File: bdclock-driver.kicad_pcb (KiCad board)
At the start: 2 copper layers, 34 parts, among them J1 PWR, J2 Ctrl, J3 Kathodes, J4 Anodes A, J5 Anodes B, J6 Anodes C, U1 NE555P, U2 LM7805_TO220, U3 74HC4017, U4 74HC595, U5 74HC595, U6 74HC595, U7 74LS138, U8 74LS138

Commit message: :hammer: Improve PCB layout
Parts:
- added REF**: MountingHole_3.2mm_M3, MountingHole:MountingHole_3.2mm_M3, F.Cu at (225.6, 101.6)
- added REF**: MountingHole_3.2mm_M3, MountingHole:MountingHole_3.2mm_M3, F.Cu at (123.6, 101.6)
- moved J1 26.3 mm to (128.2, 72.8), turned to 180 degrees
- moved C4 21.8 mm to (128.9, 96.0)
- moved D1 13.2 mm to (125.2, 92.5), turned to 90 degrees
- moved D2 11.6 mm to (121.4, 82.3), turned to -90 degrees
- moved J5 8.67 mm to (180.4, 98.4)
- moved J6 8.67 mm to (202.0, 98.4)
- moved J3 8.67 mm to (138.4, 98.4)
- moved J4 8.67 mm to (159.1, 98.4)
- moved U2 6.02 mm to (128.4, 84.2), turned to -90 degrees
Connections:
- R3 pad 1: ROW1 -> ROW3
- R4 pad 1: ROW2 -> ROW1
- R5 pad 1: ROW3 -> ROW2
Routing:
- net VCC: track 0.00 -> 185.2 mm, vias 0 -> 1
- net CLK: track 37.1 -> 69.4 mm, vias 0 -> 2
- net Net-(D1-K): track 0.00 -> 22.5 mm
- net ROW3: track 54.2 -> 74.7 mm, vias 1 -> 3
- net Net-(U3-Q3): track 0.00 -> 15.9 mm
- net A2: track 40.8 -> 56.0 mm
- net ROW2: track 34.0 -> 47.1 mm, vias 1 -> 2
- net Net-(U5-QH'): track 19.1 -> 31.3 mm, vias 0 -> 1
- net Net-(D1-A): track 0.00 -> 10.3 mm
- net Net-(U1-THR): track 31.0 -> 23.4 mm
- net Net-(J4-Pin_2): track 60.1 -> 67.6 mm, vias 1 -> 0
- net Net-(J4-Pin_3): track 53.4 -> 60.3 mm, vias 1 -> 0
- net Net-(J4-Pin_1): track 66.9 -> 73.5 mm, vias 1 -> 0
- net Net-(J5-Pin_1): track 38.3 -> 44.9 mm, vias 1 -> 0
- net Net-(J4-Pin_4): track 47.1 -> 53.4 mm, vias 1 -> 0
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- added copper zone on B.Cu, net GND
- added copper zone on F.Cu, net GND
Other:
- board outline added: 112.5 x 45.2 mm

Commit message: :art: Finalize the PCB layout
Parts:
- moved R5 6.22 mm to (152.7, 86.9)
- moved J1 4.38 mm to (125.5, 69.4), turned to -90 degrees
- moved R3 3.18 mm to (152.7, 83.8)
- moved R4 3.05 mm to (152.7, 80.8)
- moved C12 1.27 mm to (141.8, 81.9)
- moved C7 0.51 mm to (134.1, 84.3)
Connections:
- R3 pad 1: ROW3 -> ROW1
- R4 pad 1: ROW1 -> ROW2
- R5 pad 1: ROW2 -> ROW3
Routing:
- net Net-(J3-Pin_3): track 19.2 -> 13.7 mm
- net Net-(J3-Pin_2): track 15.3 -> 19.4 mm
- net Net-(J3-Pin_1): track 14.2 -> 17.3 mm
- net Net-(D1-A): track 10.3 -> 8.03 mm
- net /RST: track 67.9 -> 69.2 mm
- net VCC: track 185.2 -> 186.4 mm
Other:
- outline, holes or cut-outs redrawn
- board text added: "+9V"
- board text added: "A1"
- board text added: "A12"
- board text added: "Bulb Dial Clock Driver"
- board text added: "GND"
- board text added: "K1 H"
- board text added: "K2 M"
- board text added: "K3 S"
- board text added: "https://github.com/penguineer/bdclock-driver"
- board text added: "v1"

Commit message: :art: Geographical renumeration of all components
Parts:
- moved R4 0.13 mm to (152.7, 83.9)
- moved R6 0.13 mm to (152.7, 87.0)
- moved R3 0.13 mm to (152.7, 80.9)
- renumbered C11 to C1, C12 to C10, C7 to C11, C4 to C12, C10 to C2, C1 to C3, C3 to C4, C8 to C7, C9 to C8, C2 to C9, D2 to D1, D1 to D2, J2 to J1, J1 to J2, R2 to R1, R1 to R2, R4 to R3, R3 to R4, R6 to R5, R5 to R6, U3 to U2, U4 to U3, U5 to U4, U6 to U5, U7 to U6, U8 to U7, U2 to U8

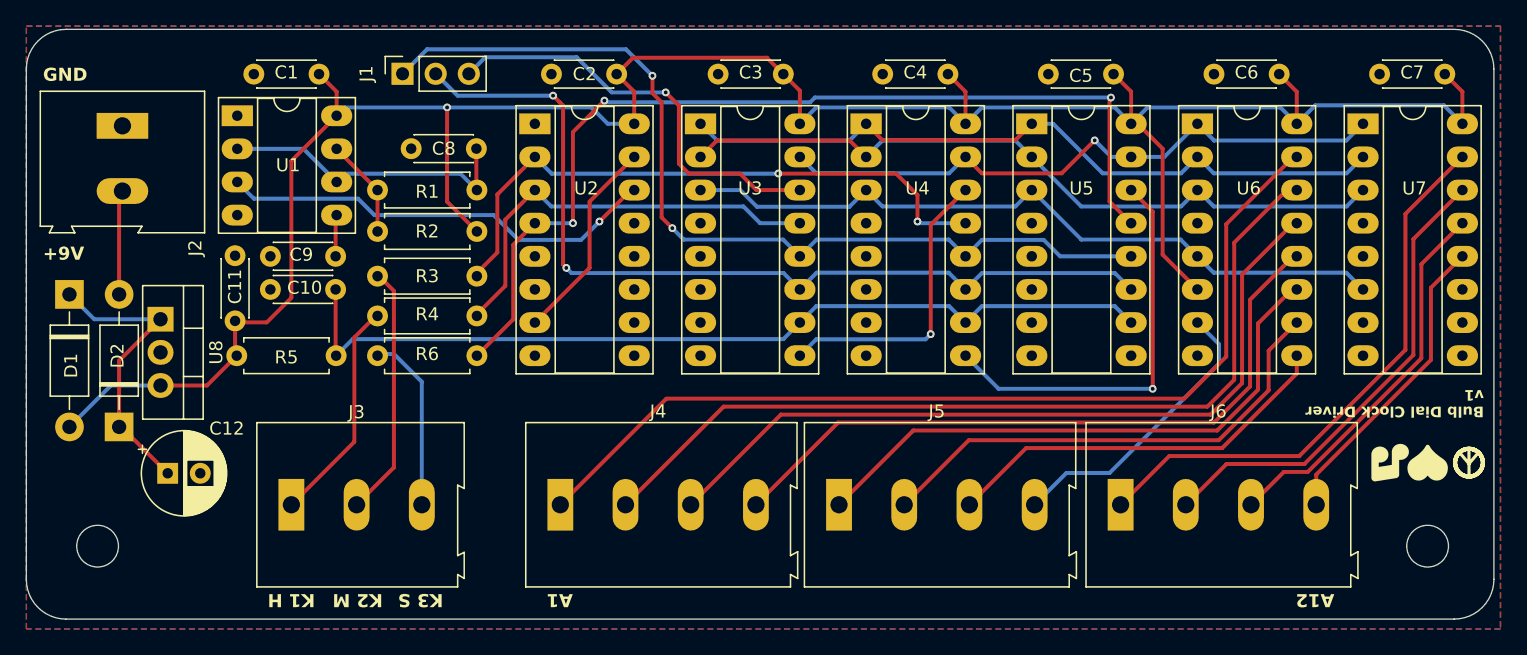
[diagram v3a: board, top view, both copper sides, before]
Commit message: :art: Place JLCPCB serial number marker and add GND to data connector
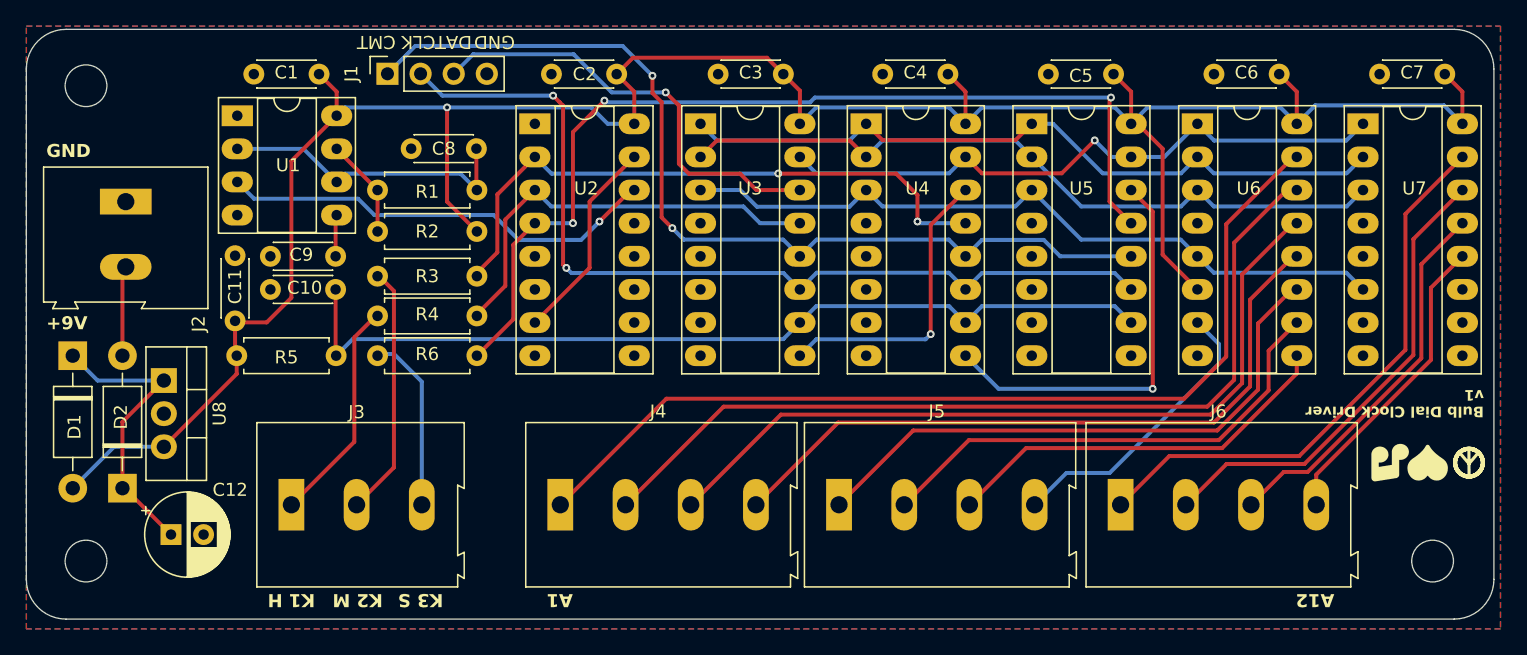
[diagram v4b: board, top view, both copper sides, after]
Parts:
- removed the REF** at (225.6, 101.6)
- removed the REF** at (123.6, 101.6)
- added REF**: MountingHole_3.2mm_M3, MountingHole:MountingHole_3.2mm_M3, F.Cu at (225.9, 102.7)
- added REF**: MountingHole_3.2mm_M3, MountingHole:MountingHole_3.2mm_M3, F.Cu at (122.7, 102.7)
- added REF**: MountingHole_3.2mm_M3, MountingHole:MountingHole_3.2mm_M3, F.Cu at (122.7, 66.3)
- J1: footprint Connector_PinSocket_2.54mm:PinSocket_1x03_P2.54mm_Vertical -> Connector_PinSocket_2.54mm:PinSocket_1x04_P2.54mm_Vertical
- moved J2 5.82 mm to (125.7, 75.2)
- moved U8 4.71 mm to (128.7, 88.9)
- moved C12 4.71 mm to (129.2, 100.7)
- moved D2 4.71 mm to (125.5, 97.2)
- moved D1 4.71 mm to (121.7, 87.0)
- moved J1 1.16 mm to (145.8, 65.4)
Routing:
- net VCC: track 186.4 -> 188.9 mm
- net COMMIT: track 71.3 -> 72.6 mm
- net DATA: track 32.7 -> 34.1 mm
- net CLK: track 69.4 -> 70.6 mm
- net Net-(D2-A): track 8.03 -> 6.92 mm
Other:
- board text added: "CLK"
- board text added: "CMT"
- board text added: "DAT"
- board text added: "JLCJLCJLCJLC"
